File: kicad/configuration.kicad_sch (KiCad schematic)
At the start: 15 parts, among them U3 MIMXRT1171DVMAB, U4 W25Q???

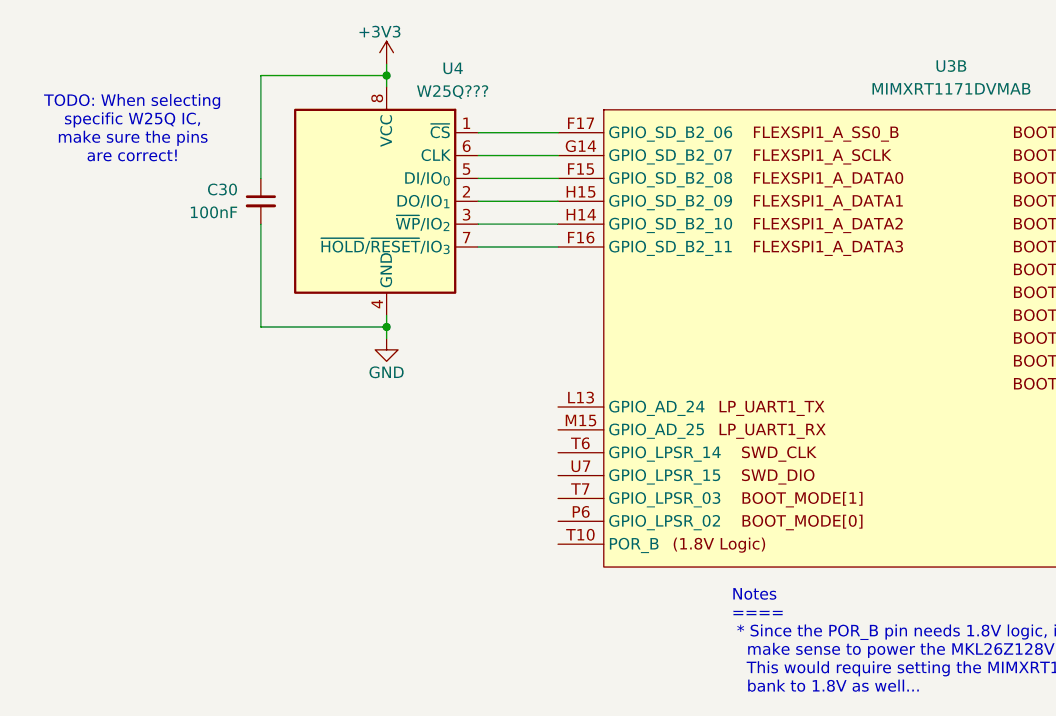
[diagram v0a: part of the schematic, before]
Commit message: reworked design to use 1.8V logic
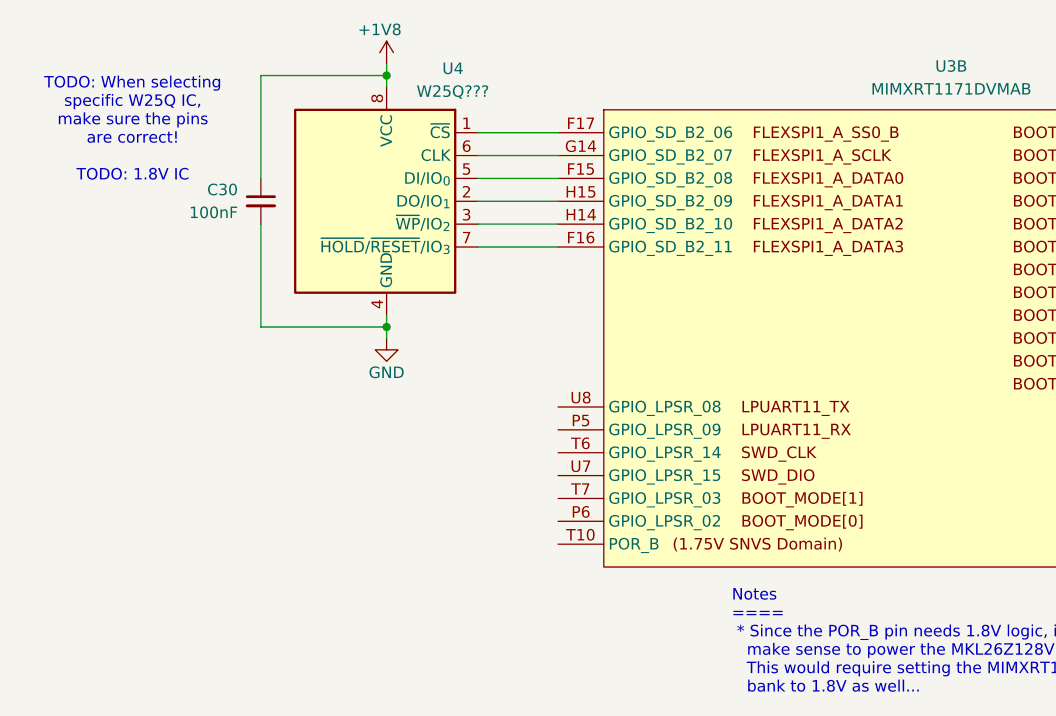
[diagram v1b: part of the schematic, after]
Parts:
- U3: footprint (none) -> Package_BGA:MAPBGA-289_14x14mm_Layout17x17_P0.8mm
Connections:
- net +3V3 renamed +1V8
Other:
- note added: "TODO: When selecting specific W25Q IC, make sure the pins are correct! TODO: 1.8V IC"
- note removed: "TODO: When selecting specific W25Q IC, make sure the pins are correct!"
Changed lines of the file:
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@@
 		(comment 2 "© 2026, Theta Machines LLC.")
 	)
-	(text "TODO: When selecting\nspecific W25Q IC,\nmake sure the pins\nare correct!"
+	(text "TODO: When selecting\nspecific W25Q IC,\nmake sure the pins\nare correct!\n\nTODO: 1.8V IC"
 		(exclude_from_sim no)
 		(at 89.916 102.616 0)
@@
 	)
 	(symbol
+		(lib_id "power:+1V0")
+		(at 118.11 95.25 0)
+		(unit 1)
+		(body_style 1)
+		(exclude_from_sim no)
+		(in_bom yes)
+		(on_board yes)
+		(in_pos_files yes)
+		(dnp no)
+		(property "Reference" "#PWR068"
+			(at 118.11 99.06 0)
+			(hide yes)
+			(show_name no)
+			(do_not_autoplace no)
+			(effects
+				(font
+					(size 1.27 1.27)
+				)
+			)
+		)
+		(property "Value" "+1V8"
+			(at 117.348 91.44 0)
+			(show_name no)
+			(do_not_autoplace no)
+			(effects
+				(font
+					(size 1.27 1.27)
+				)
+			)
+		)
+		(property "Footprint" ""
+			(at 118.11 95.25 0)
+			(hide yes)
+			(show_name no)
+			(do_not_autoplace no)
+			(effects
+				(font
+					(size 1.27 1.27)
+				)
+			)
+		)
+		(property "Datasheet" ""
+			(at 118.11 95.25 0)
+			(hide yes)
+			(show_name no)
+			(do_not_autoplace no)
+			(effects
+				(font
+					(size 1.27 1.27)
+				)
+			)
+		)
+		(property "Description" "Power symbol creates a global label with name \"+1V0\""
+			(at 118.11 95.25 0)
+			(hide yes)
+			(show_name no)
+			(do_not_autoplace no)
+			(effects
+				(font
+					(size 1.27 1.27)
+				)
+			)
+		)
+		(pin "1"
+		)
+		(instances
+			(project "DEV-G2-NANO"
+				(path "/b6656e4d-fdee-4b90-a905-7068c060191f/45e1da5b-d52f-4e94-b563-4995febadb51"
+					(reference "#PWR068")
+					(unit 1)
+				)
+			)
+		)
+	)
+	(symbol
 		(lib_id "Device:R_Small_US")
 		(at 229.87 113.03 90)
@@
 	)
 	(symbol
-		(lib_name "MIMXRT1171DVMAB_3")
 		(lib_id "project_symbols:MIMXRT1171DVMAB")
 		(at 142.24 100.33 0)
@@
 			)
 		)
-		(property "Footprint" ""
+		(property "Footprint" "Package_BGA:MAPBGA-289_14x14mm_Layout17x17_P0.8mm"
 			(at 142.24 100.33 0)
 			(hide yes)
@@
 		)
 		(pin "U10"
+		)
+		(pin "???"
+		)
+		(pin "???"
+		)
+		(pin "???"
+		)
+		(pin "???"
+		)
+		(pin "???"
+		)
+		(pin "???"
+		)
+		(pin "???"
 		)
 		(instances
@@
 					(unit 1)
 				)
-			)
-		)
-	)
-	(symbol
-		(lib_id "power:+1V0")
-		(at 118.11 95.25 0)
-		(unit 1)
-		(body_style 1)
-		(exclude_from_sim no)
-		(in_bom yes)
-		(on_board yes)
-		(in_pos_files yes)
-		(dnp no)
-		(property "Reference" "#PWR057"
-			(at 118.11 99.06 0)
-			(hide yes)
-			(show_name no)
-			(do_not_autoplace no)
-			(effects
-				(font
-					(size 1.27 1.27)
-				)
-			)
-		)
-		(property "Value" "+3V3"
-			(at 117.348 91.694 0)
-			(show_name no)
-			(do_not_autoplace no)
-			(effects
-				(font
-					(size 1.27 1.27)
-				)
-			)
-		)
-		(property "Footprint" ""
-			(at 118.11 95.25 0)
-			(hide yes)
-			(show_name no)
-			(do_not_autoplace no)
-			(effects
-				(font
-					(size 1.27 1.27)
-				)
-			)
-		)
-		(property "Datasheet" ""
-			(at 118.11 95.25 0)
-			(hide yes)
-			(show_name no)
-			(do_not_autoplace no)
-			(effects
-				(font
-					(size 1.27 1.27)
-				)
-			)
-		)
-		(property "Description" "Power symbol creates a global label with name \"+1V0\""
-			(at 118.11 95.25 0)
-			(hide yes)
-			(show_name no)
-			(do_not_autoplace no)
-			(effects
-				(font
-					(size 1.27 1.27)
-				)
-			)
-		)
-		(pin "1"
-		)
-		(instances
-			(project "DEV-G2-NANO"
-				(path "/b6656e4d-fdee-4b90-a905-7068c060191f/45e1da5b-d52f-4e94-b563-4995febadb51"
-					(reference "#PWR057")
-					(unit 1)
-				)

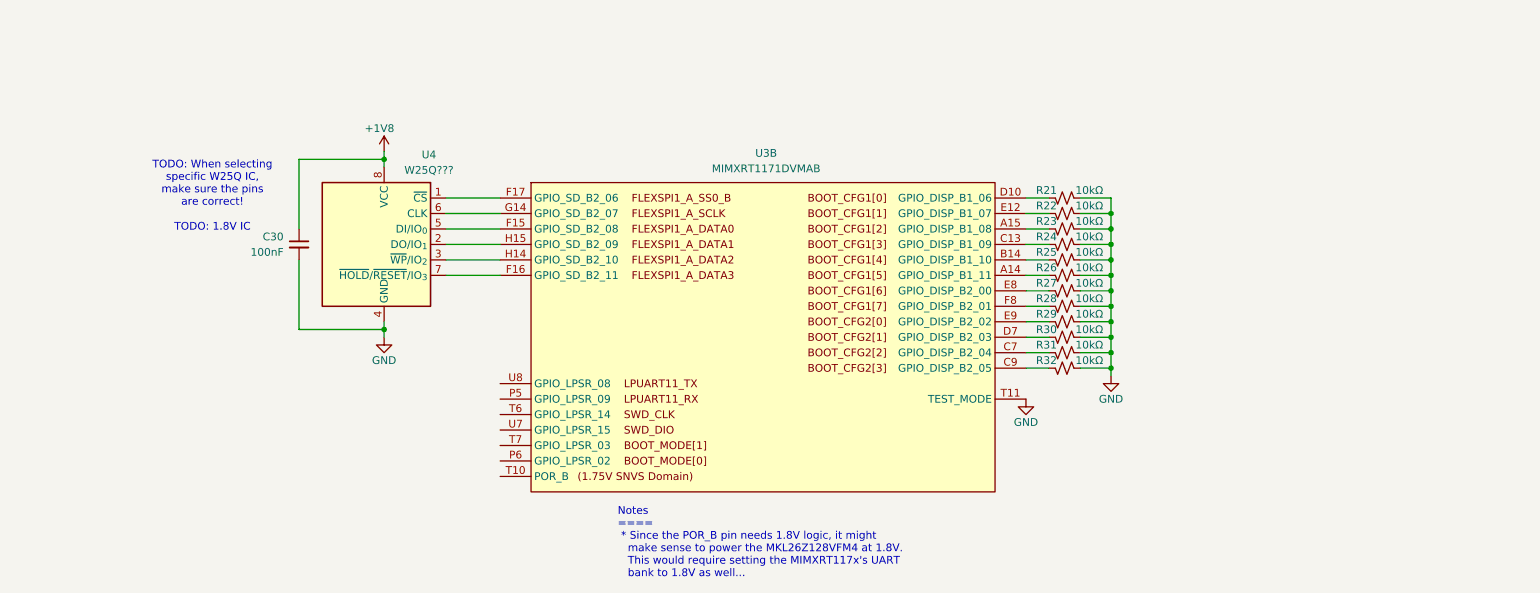
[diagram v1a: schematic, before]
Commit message: added user button and LED
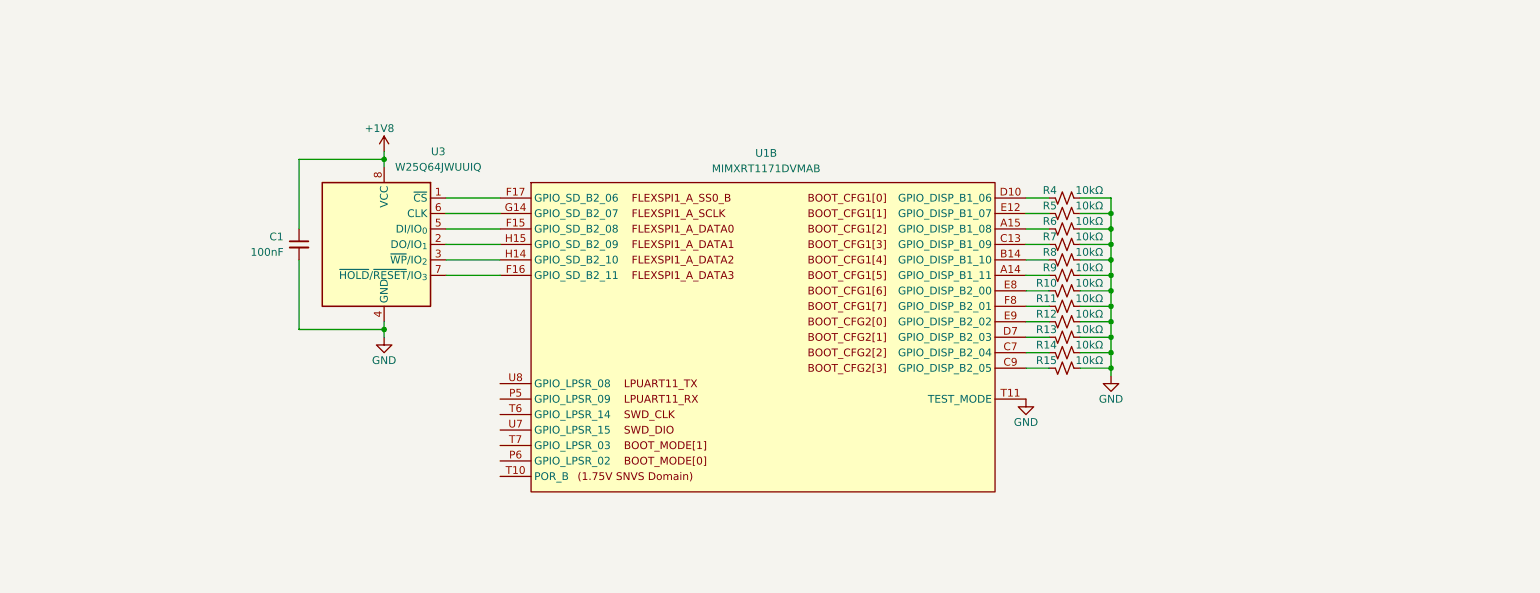
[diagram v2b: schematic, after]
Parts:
- U3: renamed from U4; value W25Q??? -> W25Q64JWUUIQ
- renumbered C30 to C1, R27 to R10, R28 to R11, R29 to R12, R30 to R13, R31 to R14, R32 to R15, R21 to R4, R22 to R5, R23 to R6, R24 to R7, R25 to R8, R26 to R9, U3 to U1
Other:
- note removed: "Notes ==== * Since the POR_B pin needs 1.8V logic, it might make sense to power the MKL26Z128VFM4 at 1.8V. This would require setting the MIMXRT117x's UART bank to 1.8V as well..."
- note removed: "TODO: When selecting specific W25Q IC, make sure the pins are correct! TODO: 1.8V IC"
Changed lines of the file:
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@@
 		(comment 2 "© 2026, Theta Machines LLC.")
-	)
-	(text "TODO: When selecting\nspecific W25Q IC,\nmake sure the pins\nare correct!\n\nTODO: 1.8V IC"
-		(exclude_from_sim no)
-		(at 89.916 102.616 0)
-		(effects
-			(font
-				(size 1.27 1.27)
-			)
-		)
-	)
-	(text "Notes\n====\n * Since the POR_B pin needs 1.8V logic, it might\n   make sense to power the MKL26Z128VFM4 at 1.8V.\n   This would require setting the MIMXRT117x's UART\n   bank to 1.8V as well..."
-		(exclude_from_sim no)
-		(at 156.464 159.512 0)
-		(effects
-			(font
-				(size 1.27 1.27)
-			)
-			(justify left)
-		)
 	)
 	(junction
@@
 		(in_pos_files yes)
 		(dnp no)
-		(property "Reference" "R32"
+		(property "Reference" "R15"
 			(at 228.6 129.54 90)
 			(show_name no)
@@
 			(project "DEV-G2-NANO"
 				(path "/b6656e4d-fdee-4b90-a905-7068c060191f/45e1da5b-d52f-4e94-b563-4995febadb51"
-					(reference "R32")
+					(reference "R15")
 					(unit 1)
 				)
@@
 		(in_pos_files yes)
 		(dnp no)
-		(property "Reference" "R29"
+		(property "Reference" "R12"
 			(at 228.6 121.92 90)
 			(show_name no)
@@
 			(project "DEV-G2-NANO"
 				(path "/b6656e4d-fdee-4b90-a905-7068c060191f/45e1da5b-d52f-4e94-b563-4995febadb51"
-					(reference "R29")
+					(reference "R12")
 					(unit 1)
 				)
@@
 		(in_pos_files yes)
 		(dnp no)
-		(property "Reference" "R30"
+		(property "Reference" "R13"
 			(at 228.6 124.46 90)
 			(show_name no)
@@
 			(project "DEV-G2-NANO"
 				(path "/b6656e4d-fdee-4b90-a905-7068c060191f/45e1da5b-d52f-4e94-b563-4995febadb51"
-					(reference "R30")
+					(reference "R13")
 					(unit 1)
 				)
@@
 		(in_pos_files yes)
 		(dnp no)
-		(property "Reference" "U4"
-			(at 125.476 95.758 0)
-			(show_name no)
-			(do_not_autoplace no)
-			(effects
-				(font
-					(size 1.27 1.27)
-				)
-			)
-		)
-		(property "Value" "W25Q???"
-			(at 125.476 98.298 0)
+		(property "Reference" "U3"
+			(at 127 95.25 0)
+			(show_name no)
+			(do_not_autoplace no)
+			(effects
+				(font
+					(size 1.27 1.27)
+				)
+			)
+		)
+		(property "Value" "W25Q64JWUUIQ"
+			(at 127 97.79 0)
 			(show_name no)
 			(do_not_autoplace no)
@@
 			(project "DEV-G2-NANO"
 				(path "/b6656e4d-fdee-4b90-a905-7068c060191f/45e1da5b-d52f-4e94-b563-4995febadb51"
-					(reference "U4")
+					(reference "U3")
 					(unit 1)
 				)
@@
 		(in_pos_files yes)
 		(dnp no)
-		(property "Reference" "#PWR058"
+		(property "Reference" "#PWR010"
 			(at 118.11 132.08 0)
 			(hide yes)
@@
 			(project "DEV-G2-NANO"
 				(path "/b6656e4d-fdee-4b90-a905-7068c060191f/45e1da5b-d52f-4e94-b563-4995febadb51"
-					(reference "#PWR058")
+					(reference "#PWR010")
 					(unit 1)
 				)
@@
 		(in_pos_files yes)
 		(dnp no)
-		(property "Reference" "R23"
+		(property "Reference" "R6"
 			(at 228.6 106.68 90)
 			(show_name no)
@@
 			(project "DEV-G2-NANO"
 				(path "/b6656e4d-fdee-4b90-a905-7068c060191f/45e1da5b-d52f-4e94-b563-4995febadb51"
-					(reference "R23")
+					(reference "R6")
 					(unit 1)
 				)
@@
 		(in_pos_files yes)
 		(dnp no)
-		(property "Reference" "#PWR068"
+		(property "Reference" "#PWR09"
 			(at 118.11 99.06 0)
 			(hide yes)
@@
 			(project "DEV-G2-NANO"
 				(path "/b6656e4d-fdee-4b90-a905-7068c060191f/45e1da5b-d52f-4e94-b563-4995febadb51"
-					(reference "#PWR068")
+					(reference "#PWR09")
 					(unit 1)
 				)
@@
 		(in_pos_files yes)
 		(dnp no)
-		(property "Reference" "R25"
+		(property "Reference" "R8"
 			(at 228.6 111.76 90)
 			(show_name no)
@@
 			(project "DEV-G2-NANO"
 				(path "/b6656e4d-fdee-4b90-a905-7068c060191f/45e1da5b-d52f-4e94-b563-4995febadb51"
-					(reference "R25")
+					(reference "R8")
 					(unit 1)
 				)
@@
 		(in_pos_files yes)
 		(dnp no)
-		(property "Reference" "#PWR056"
+		(property "Reference" "#PWR011"
 			(at 223.52 142.24 0)
 			(hide yes)
@@
 			(project "DEV-G2-NANO"
 				(path "/b6656e4d-fdee-4b90-a905-7068c060191f/45e1da5b-d52f-4e94-b563-4995febadb51"
-					(reference "#PWR056")
+					(reference "#PWR011")
 					(unit 1)
 				)
@@
 		(in_pos_files yes)
 		(dnp no)
-		(property "Reference" "#PWR055"
+		(property "Reference" "#PWR012"
 			(at 237.49 138.43 0)
 			(hide yes)
@@
 			(project "DEV-G2-NANO"
 				(path "/b6656e4d-fdee-4b90-a905-7068c060191f/45e1da5b-d52f-4e94-b563-4995febadb51"
-					(reference "#PWR055")
+					(reference "#PWR012")
 					(unit 1)
 				)
@@
 		(in_pos_files yes)
 		(dnp no)
-		(property "Reference" "R27"
+		(property "Reference" "R10"
 			(at 228.6 116.84 90)
 			(show_name no)
@@
 			(project "DEV-G2-NANO"
 				(path "/b6656e4d-fdee-4b90-a905-7068c060191f/45e1da5b-d52f-4e94-b563-4995febadb51"
-					(reference "R27")
+					(reference "R10")
 					(unit 1)
 				)
@@
 		(in_pos_files yes)
 		(dnp no)
-		(property "Reference" "R31"
+		(property "Reference" "R14"
 			(at 228.6 127 90)
 			(show_name no)
@@
 			(project "DEV-G2-NANO"
 				(path "/b6656e4d-fdee-4b90-a905-7068c060191f/45e1da5b-d52f-4e94-b563-4995febadb51"
-					(reference "R31")
+					(reference "R14")
 					(unit 1)
 				)
@@
 		(in_pos_files yes)
 		(dnp no)
-		(property "Reference" "R24"
+		(property "Reference" "R7"
 			(at 228.6 109.22 90)
 			(show_name no)
@@
 			(project "DEV-G2-NANO"
 				(path "/b6656e4d-fdee-4b90-a905-7068c060191f/45e1da5b-d52f-4e94-b563-4995febadb51"
-					(reference "R24")
+					(reference "R7")
 					(unit 1)
 				)
@@
 		(in_pos_files yes)
 		(dnp no)
-		(property "Reference" "R22"
+		(property "Reference" "R5"
 			(at 228.6 104.14 90)
 			(show_name no)
@@
 			(project "DEV-G2-NANO"
 				(path "/b6656e4d-fdee-4b90-a905-7068c060191f/45e1da5b-d52f-4e94-b563-4995febadb51"
-					(reference "R22")
+					(reference "R5")
 					(unit 1)
 				)
@@
 		(in_pos_files yes)
 		(dnp no)
-		(property "Reference" "U3"
+		(property "Reference" "U1"
 			(at 180.848 95.504 0)
 			(show_name no)
@@
 			(project "DEV-G2-NANO"
 				(path "/b6656e4d-fdee-4b90-a905-7068c060191f/45e1da5b-d52f-4e94-b563-4995febadb51"
-					(reference "U3")
+					(reference "U1")
 					(unit 2)
 				)
@@
 		(in_pos_files yes)
 		(dnp no)
-		(property "Reference" "R28"
+		(property "Reference" "R11"
 			(at 228.6 119.38 90)
 			(show_name no)
@@
 			(project "DEV-G2-NANO"
 				(path "/b6656e4d-fdee-4b90-a905-7068c060191f/45e1da5b-d52f-4e94-b563-4995febadb51"
-					(reference "R28")
+					(reference "R11")
 					(unit 1)
 				)
@@
 		(in_pos_files yes)
 		(dnp no)
-		(property "Reference" "R26"
+		(property "Reference" "R9"
 			(at 228.6 114.3 90)
 			(show_name no)
@@
 			(project "DEV-G2-NANO"
 				(path "/b6656e4d-fdee-4b90-a905-7068c060191f/45e1da5b-d52f-4e94-b563-4995febadb51"
-					(reference "R26")
+					(reference "R9")
 					(unit 1)
 				)
@@
 		(in_pos_files yes)
 		(dnp no)
-		(property "Reference" "C30"
+		(property "Reference" "C1"
 			(at 101.6 109.2262 0)
 			(show_name no)
@@
 			(project "DEV-G2-NANO"
 				(path "/b6656e4d-fdee-4b90-a905-7068c060191f/45e1da5b-d52f-4e94-b563-4995febadb51"
-					(reference "C30")
+					(reference "C1")
 					(unit 1)
 				)
@@
 		(in_pos_files yes)
 		(dnp no)
-		(property "Reference" "R21"
+		(property "Reference" "R4"
 			(at 228.6 101.6 90)
 			(show_name no)
@@
 			(project "DEV-G2-NANO"
 				(path "/b6656e4d-fdee-4b90-a905-7068c060191f/45e1da5b-d52f-4e94-b563-4995febadb51"
-					(reference "R21")
+					(reference "R4")
 					(unit 1)
 				)

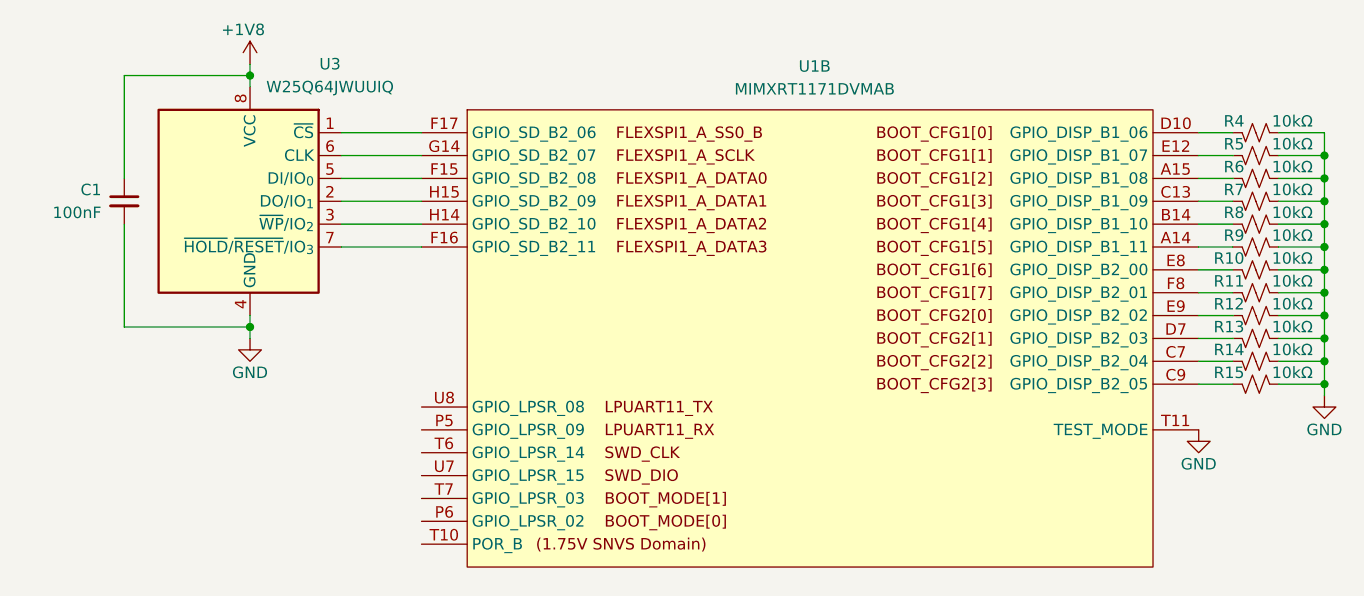
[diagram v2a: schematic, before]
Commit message: added 3.3V and 1.8V buck converters to schematic
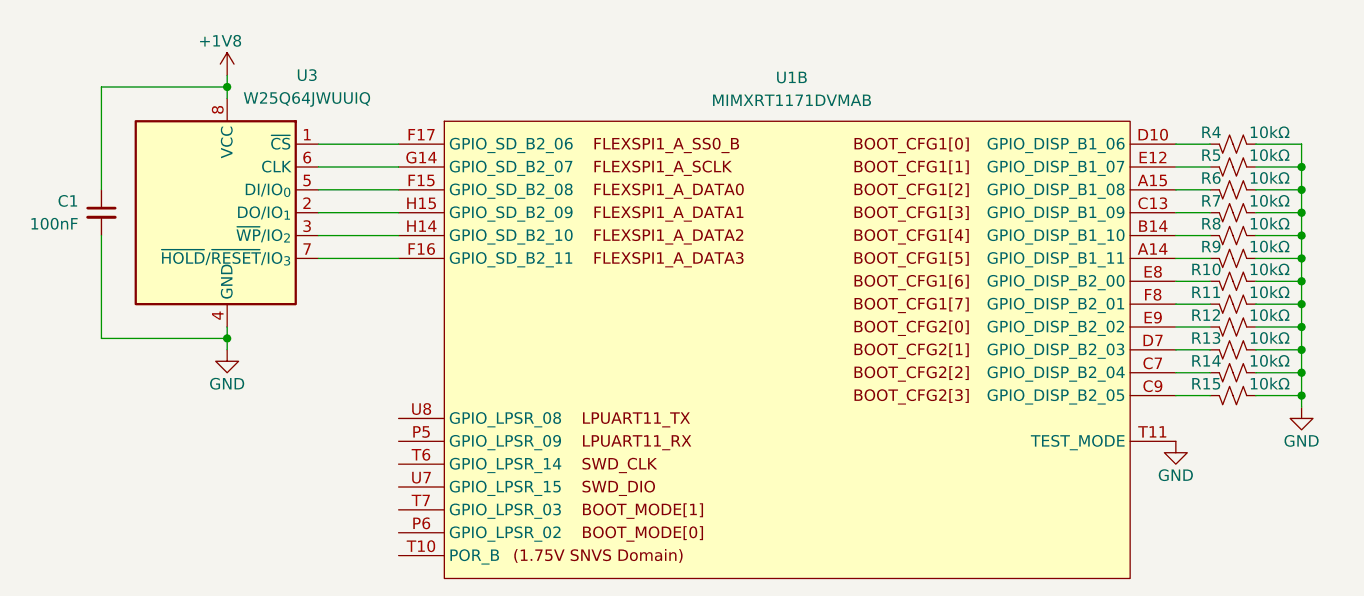
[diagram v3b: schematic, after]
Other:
- moved on the sheet: C1, R10, R11, R12, R13, R14, R15, R4, R5, R6, R7, R8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
